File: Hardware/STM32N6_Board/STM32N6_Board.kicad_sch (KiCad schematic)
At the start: 0 parts

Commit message: Created the inital schematic for the Power unit
- Power unit schematic completed but NOT CHECKED.
- Also, V_DDA1V8PMU must be connected to V_DD1V8 somehow through a
  ferrite
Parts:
- added C1: 4.7u, symbol Device:C_Small_US
- added C10, C9: 10u, symbol Device:C_Small_US
- added C11, C12, C20, C23, C24, C25, C26, C27, C28, C29: 1u, symbol Device:C_Small_US
- added C13, C14, C15, C16, C17, C18, C19, C21, C22, C30, C31, C32, C33, C34, C7, C8: 100n, symbol Device:C_Small_US
- added C2: 2.2n, symbol Device:C_Small_US
- added C3, C4, C5, C6: 15u, symbol Device:C_Small_US
- added L1: 1u, symbol Device:L_Small
- added L2: 2.2n, symbol Device:L_Small
- added R2: 2, symbol Device:R_Small_US
- added U1: ~, symbol STM32N6_Symbols:STM32N657I0H3Q
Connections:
- new net: C1.2, U1.D1 (V08CAP)
- new net: C2.1, R2.2
- new net GND: C1.1, C10.2, C11.2, C12.2, C13.2, C14.2, C15.2, C16.2, C17.2, C18.2, C19.2, C2.2, C20.2, C21.2, C22.2, C23.2, C24.2, C25.2, C26.2, C27.2, C28.2, C29.2, C3.2, C30.2, C31.2, C32.2, C33.2, C34.2, C4.2, C5.2, C6.2, C7.2, C8.2, C9.2, U1.A14 (VSS), U1.E2 (VSSAPMU), U1.E7 (VSS), U1.F1 (VSSSMPS), U1.F10 (VSS), U1.F2 (VSSSMPS), U1.F3 (VSSSMPS), U1.F4 (VSSSMPS), U1.F5 (VSSAON), U1.H10 (VSS), U1.H11 (VSS), U1.K10 (VSS), U1.K5 (VSS), U1.M4 (VSSA), U1.N1 (VREF-), U1.P1 (VSS), U1.P14 (VSS)
- new net VDD: C13.1, C14.1, C15.1, C16.1, C17.1, C18.1, C19.1, U1.C2 (VBAT), U1.E8 (VDDIO4), U1.E9 (VDDIO4), U1.G10 (VDD), U1.G11 (VDD), U1.G12 (VDD), U1.J10 (VDDIO3), U1.J11 (VDDIO3)
- new net VDD1V8: L2.2
- new net VDD3V3: C29.1, U1.A4 (VDD33USB)
- new net VDDA1V8: C31.1, C32.1, C33.1, C34.1, U1.D4 (VDDA18USB), U1.L4 (VDDA18PLL), U1.M3 (VDDA18ADC), U1.P5 (VDDA18CSI)
- new net VDDA1V8PMU: C30.1, U1.E1 (VDDA18PMU)
- new net VDDA1V8_AON: C22.1, U1.E5 (VDDA18AON)
- new net VDDCORE: C23.1, C24.1, C25.1, C26.1, C27.1, C28.1, U1.K6 (VDDCORE), U1.K7 (VDDCORE), U1.K8 (VDDCORE), U1.K9 (VDDCORE), U1.L7 (VDDCORE), U1.N6 (VDDCSI)
- new net VDDSMPS: C10.1, C11.1, C12.1, C7.1, C8.1, C9.1, L2.1, U1.H1 (VDDSMPS), U1.H2 (VDDSMPS), U1.H3 (VDDSMPS), U1.H4 (VDDSMPS)
- new net VFBSMPS: C3.1, C4.1, C5.1, C6.1, L1.2, U1.D2 (VFBSMPS)
- new net VLXSMPS: L1.1, R2.1, U1.G1 (VLXSMPS), U1.G2 (VLXSMPS), U1.G3 (VLXSMPS), U1.G4 (VLXSMPS)
- new net VREFP: C20.1, C21.1, U1.M1 (VREF+)
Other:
- note added: "STM32N6 Power Unit"

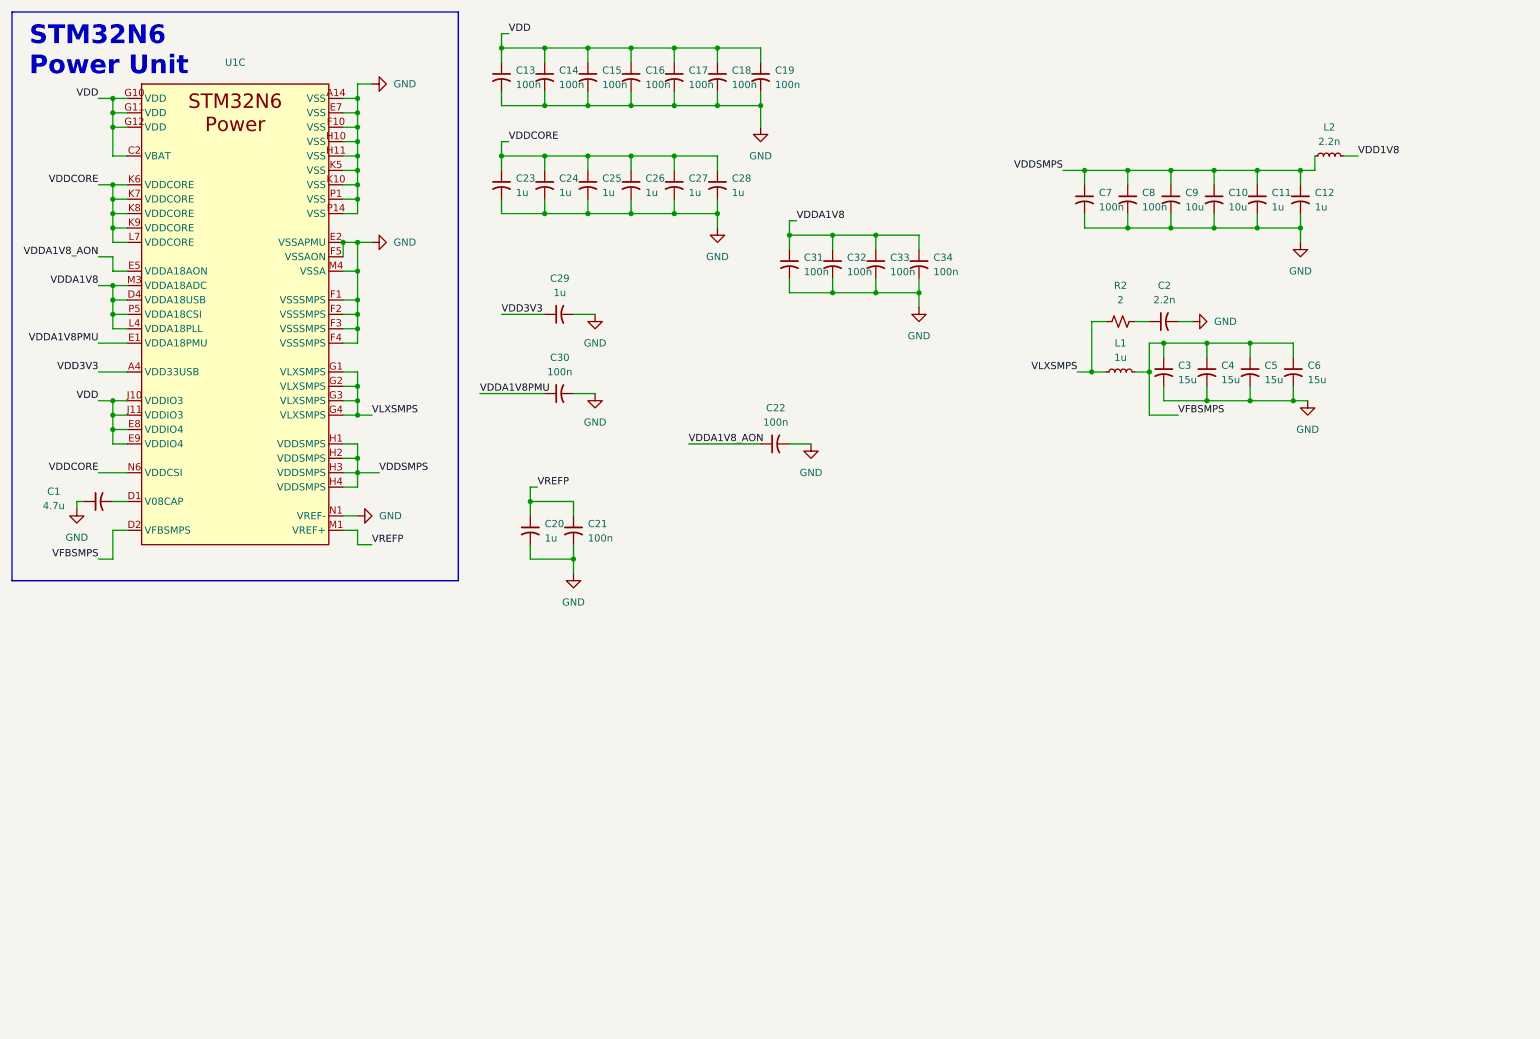
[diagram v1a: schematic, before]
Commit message: Completed and checked the Power unit of the schematic
- Completed the schematic with LDOs and Bucks as needed
- Double checked all netlists.
- Added relevant datasheets
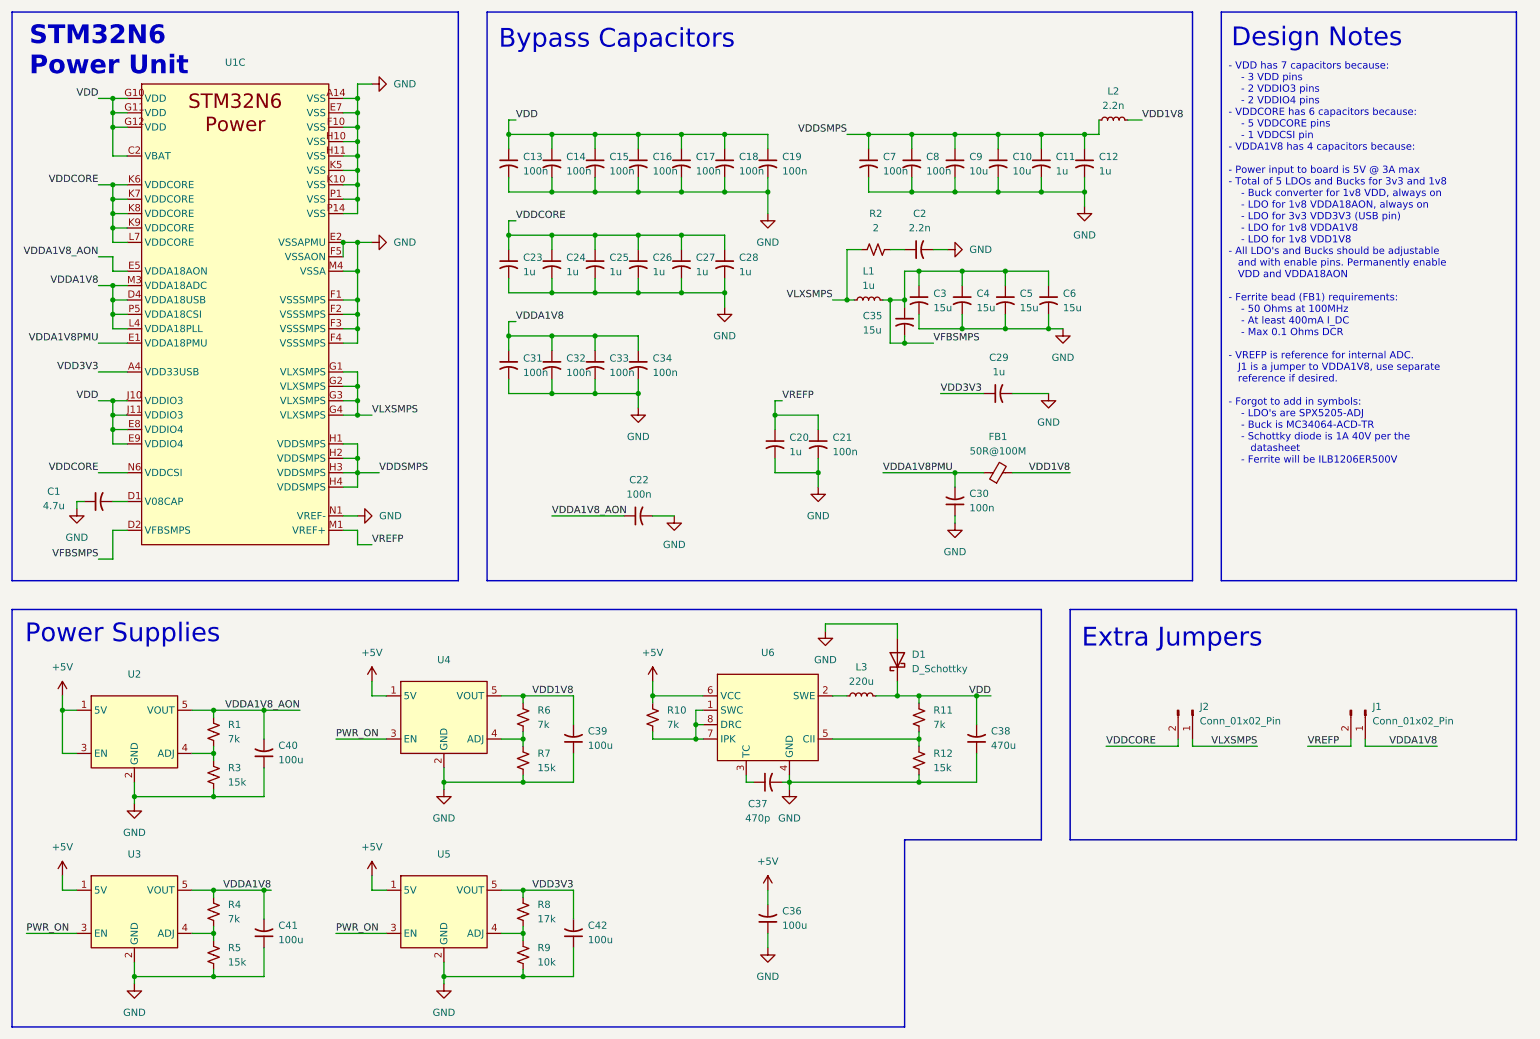
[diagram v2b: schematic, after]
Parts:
- added C35: 15u, symbol Device:C_Small_US
- added C36, C39, C40, C41, C42: 100u, symbol Device:C_Small_US
- added C37: 470p, symbol Device:C_Small_US
- added C38: 470u, symbol Device:C_Small_US
- added D1: D_Schottky, symbol Device:D_Schottky
- added FB1: 50R@100M, symbol Device:FerriteBead_Small
- added J1, J2: Conn_01x02_Pin, symbol Connector:Conn_01x02_Pin
- added L3: 220u, symbol Device:L_Small
- added R1, R10, R11, R4, R6: 7k, symbol Device:R_Small_US
- added R12, R3, R5, R7: 15k, symbol Device:R_Small_US
- added R8: 17k, symbol Device:R_Small_US
- added R9: 10k, symbol Device:R_Small_US
- added U2, U3, U4, U5: ~, symbol STM32N6_Symbols:SPX5205-ADJ
- added U6: ~, symbol STM32N6_Symbols:MC34063ACD-TR
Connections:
- net GND: now also C30.1, C36.1, C37.2, C38.1, C39.1, C40.1, C41.1, C42.1, D1.2 (A), R12.2, R3.2, R5.2, R7.2, R9.2, U2.2 (GND), U3.2 (GND), U4.2 (GND), U5.2 (GND), U6.4 (GND); no longer C30.2
- net VDD: now also C38.2, D1.1 (K), L3.2, R11.1
- net VDD1V8: now also C39.2, FB1.2, R6.1, U4.5 (VOUT)
- net VDD3V3: now also C42.2, R8.1, U5.5 (VOUT)
- net VDDA1V8: now also C41.2, J1.1 (Pin_1), R4.1, U3.5 (VOUT)
- net VDDA1V8PMU: now also C30.2, FB1.1; no longer C30.1
- net VDDA1V8_AON: now also C40.2, R1.1, U2.5 (VOUT)
- net VDDCORE: now also J2.2 (Pin_2)
- net VFBSMPS: now also C35.1, C35.2
- net VLXSMPS: now also J2.1 (Pin_1)
- net VREFP: now also J1.2 (Pin_2)
- new net: R8.2, R9.1, U5.4 (ADJ)
- new net: R4.2, R5.1, U3.4 (ADJ)
- new net: R11.2, R12.1, U6.5 (CII)
- new net: R1.2, R3.1, U2.4 (ADJ)
- new net: C37.1, U6.3 (TC)
- new net: R10.2, U6.1 (SWC), U6.7 (IPK), U6.8 (DRC)
- new net: L3.1, U6.2 (SWE)
- new net: R6.2, R7.1, U4.4 (ADJ)
- new net +5V: C36.2, R10.1, U2.1 (5V), U2.3 (EN), U3.1 (5V), U4.1 (5V), U5.1 (5V), U6.6 (VCC)
- new net PWR_ON: U3.3 (EN), U4.3 (EN), U5.3 (EN)
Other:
- note added: "- VDD has 7 capacitors because: - 3 VDD pins - 2 VDDIO3 pins - 2 VDDIO4 pins - VDDCORE has 6 capacitors because: - 5 VDDCORE pins - 1 VDDCSI pin - VDDA1V8 has 4 capacitors because: - Power input to board is 5V @ 3A max - Total of 5 LDOs and Bucks for 3v3 and 1v8 - Buck converter for 1v8 VDD, always on - LDO for 1v8 VDDA18AON, always on - LDO for 3v3 VDD3V3 (USB pin) - LDO for 1v8 VDDA1V8 - LDO fo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"
- note added: "Bypass Capacitors"
- note added: "Design Notes"
- note added: "Extra Jumpers"
- note added: "Power Supplies"
- company: (none) -> SolarVision
- title: (none) -> SolarVision Mower - STM32N6 Power Units
- moved on the sheet: C10, C11, C12, C13, C14, C15, C16, C17, C18, C19, C2, C20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

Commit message: Added lots of stuff
- Completed most of power schematic YET TO ADD PWR LEDS
- Completed bus wiring of the GPIO unit
- Completed wiring of XSPI NOR Flash
- Beginning wiring of Analog unit next
- Redrew MX25LM symbol since pin numbers didn't match up
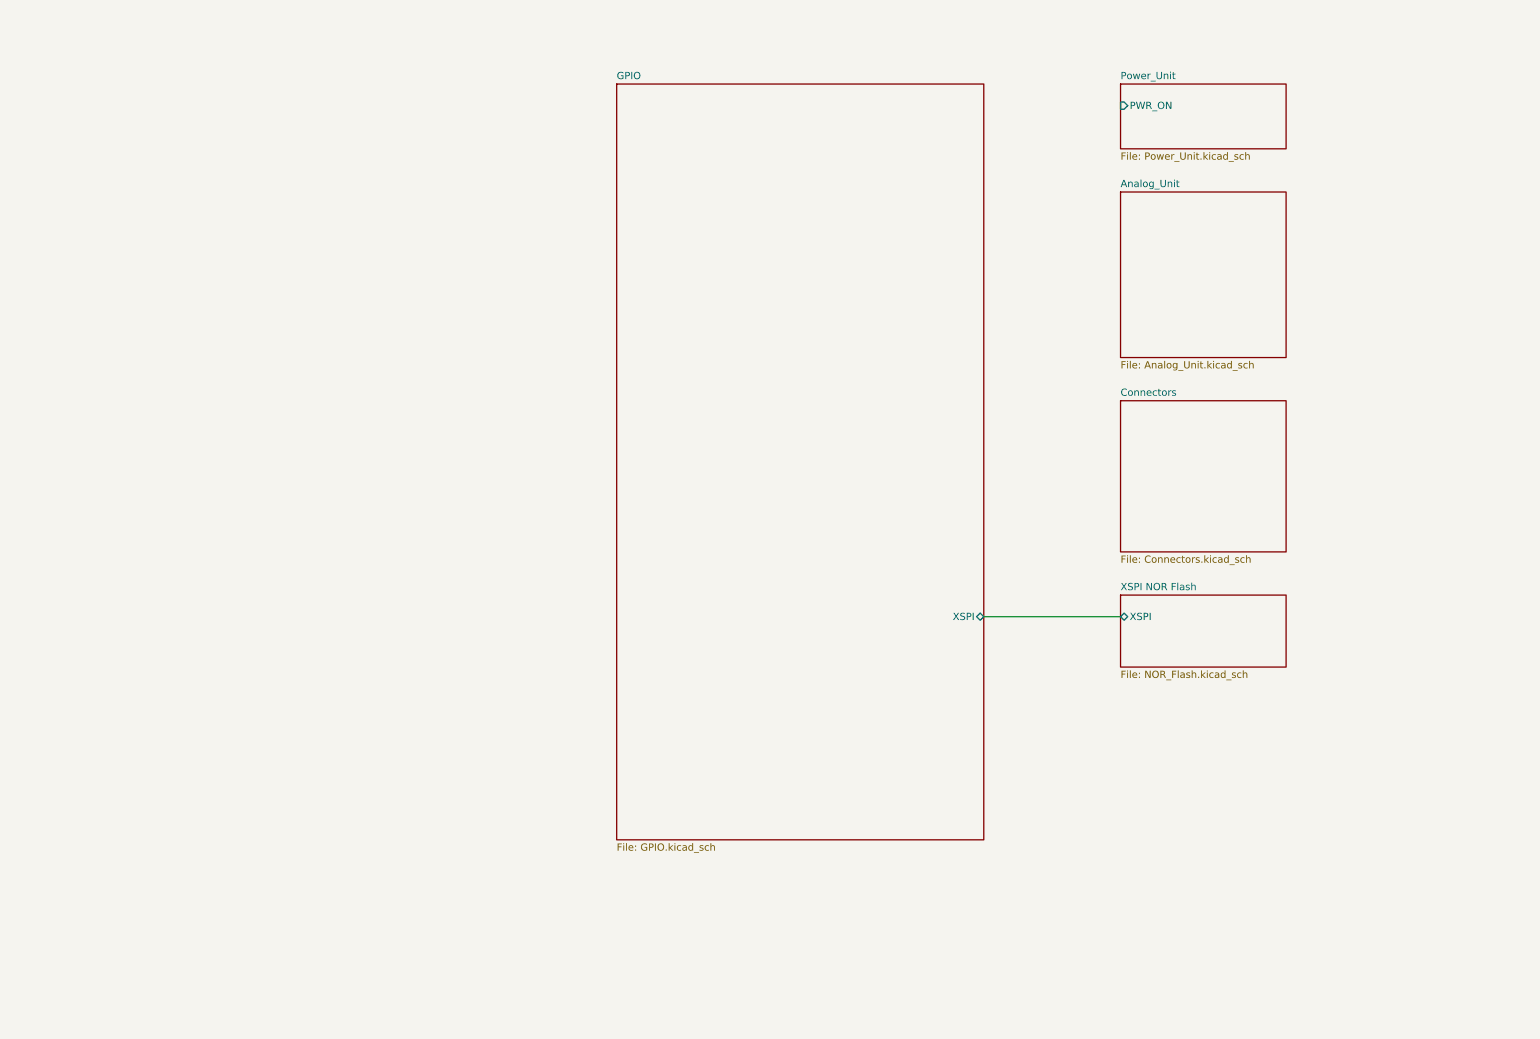
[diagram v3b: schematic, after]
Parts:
- removed C1: 4.7u, symbol Device:C_Small_US
- removed C10, C9: 10u, symbol Device:C_Small_US
- removed C11, C12, C20, C23, C24, C25, C26, C27, C28, C29: 1u, symbol Device:C_Small_US
- removed C13, C14, C15, C16, C17, C18, C19, C21, C22, C30, C31, C32, C33, C34, C7, C8: 100n, symbol Device:C_Small_US
- removed C2: 2.2n, symbol Device:C_Small_US
- removed C3, C35, C4, C5, C6: 15u, symbol Device:C_Small_US
- removed C36, C39, C40, C41, C42: 100u, symbol Device:C_Small_US
- removed C37: 470p, symbol Device:C_Small_US
- removed C38: 470u, symbol Device:C_Small_US
- removed D1: D_Schottky, symbol Device:D_Schottky
- removed FB1: 50R@100M, symbol Device:FerriteBead_Small
- removed J1, J2: Conn_01x02_Pin, symbol Connector:Conn_01x02_Pin
- removed L1: 1u, symbol Device:L_Small
- removed L2: 2.2n, symbol Device:L_Small
- removed L3: 220u, symbol Device:L_Small
- removed R1, R10, R11, R4, R6: 7k, symbol Device:R_Small_US
- removed R12, R3, R5, R7: 15k, symbol Device:R_Small_US
- removed R2: 2, symbol Device:R_Small_US
- removed R8: 17k, symbol Device:R_Small_US
- removed R9: 10k, symbol Device:R_Small_US
- removed U1: ~, symbol STM32N6_Symbols:STM32N657I0H3Q
- removed U2, U3, U4, U5: ~, symbol STM32N6_Symbols:SPX5205-ADJ
- removed U6: ~, symbol STM32N6_Symbols:MC34063ACD-TR
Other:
- added sheet Analog_Unit (Analog_Unit.kicad_sch)
- added sheet Connectors (Connectors.kicad_sch)
- added sheet GPIO (GPIO.kicad_sch)
- added sheet Power_Unit (Power_Unit.kicad_sch)
- added sheet XSPI NOR Flash (NOR_Flash.kicad_sch)
- note removed: "- VDD has 7 capacitors because: - 3 VDD pins - 2 VDDIO3 pins - 2 VDDIO4 pins - VDDCORE has 6 capacitors because: - 5 VDDCORE pins - 1 VDDCSI pin - VDDA1V8 has 4 capacitors because: - Power input to board is 5V @ 3A max - Total of 5 LDOs and Bucks for 3v3 and 1v8 - Buck converter for 1v8 VDD, always on - LDO for 1v8 VDDA18AON, always on - LDO for 3v3 VDD3V3 (USB pin) - LDO for 1v8 VDDA1V8 - LDO fo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"
- note removed: "Bypass Capacitors"
- note removed: "Design Notes"
- note removed: "Extra Jumpers"
- note removed: "Power Supplies"
- note removed: "STM32N6 Power Unit"
- title: SolarVision Mower - STM32N6 Power Units -> SolarVision Mower - STM32N6 Board
